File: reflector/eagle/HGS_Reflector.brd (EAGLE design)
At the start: 100 x 100 mm, 42 parts, among them J1 U.FL, J2 USB_MINI-B_SMT, U1 LP2985XX-N, U2 LP2985XX-N

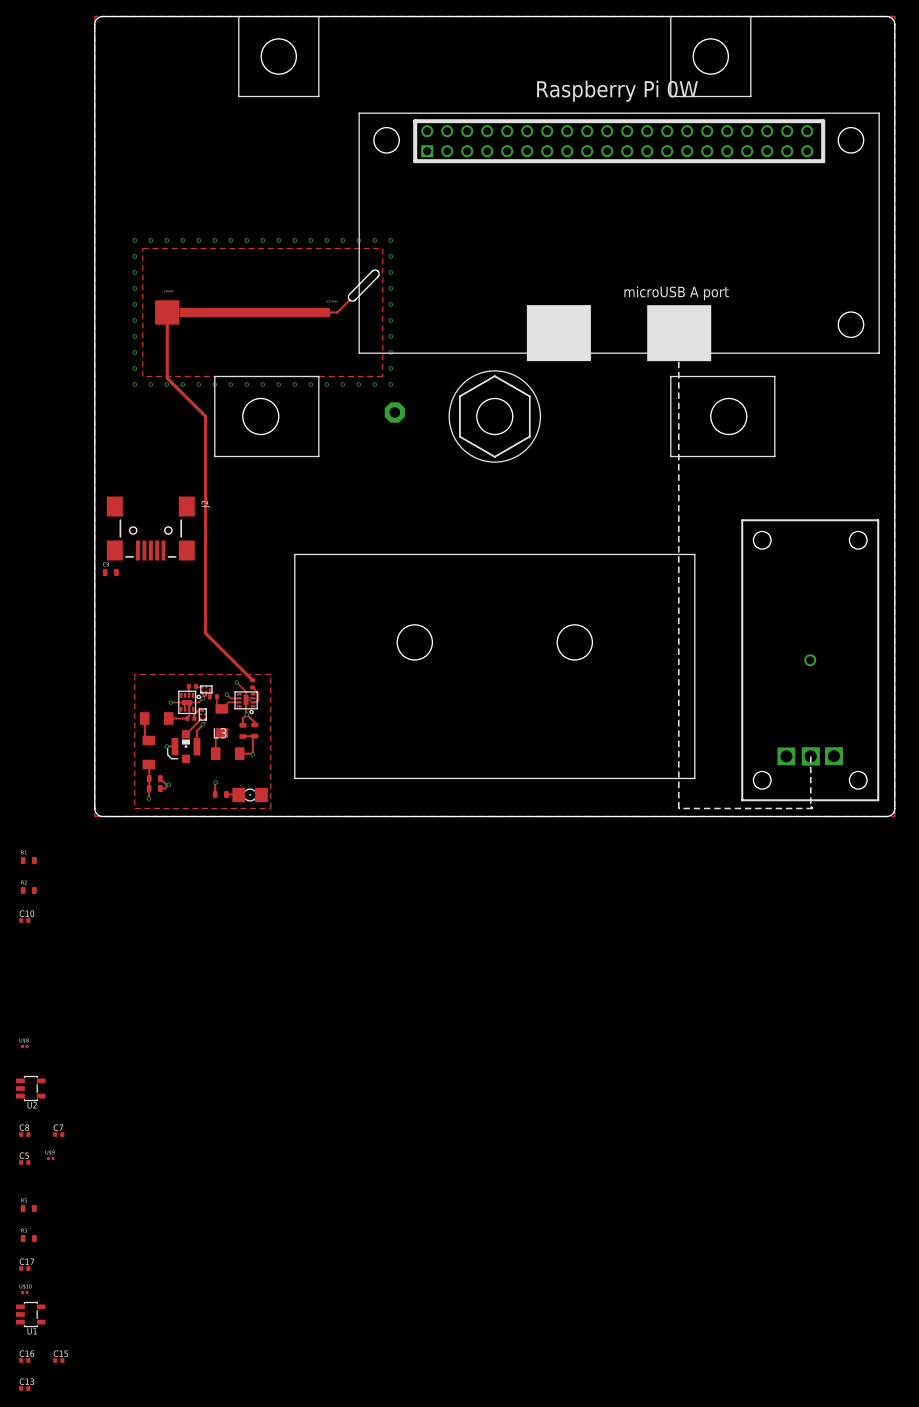
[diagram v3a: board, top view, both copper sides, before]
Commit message: Update for Oliver's series of RF tests to see if we can really do this HGS thing. Took Nohl's board and cleaned it up a bit; the LNA and PS and other things are just for fun; the real purpose of this board is for testing the helical and for testing mechanical fit.
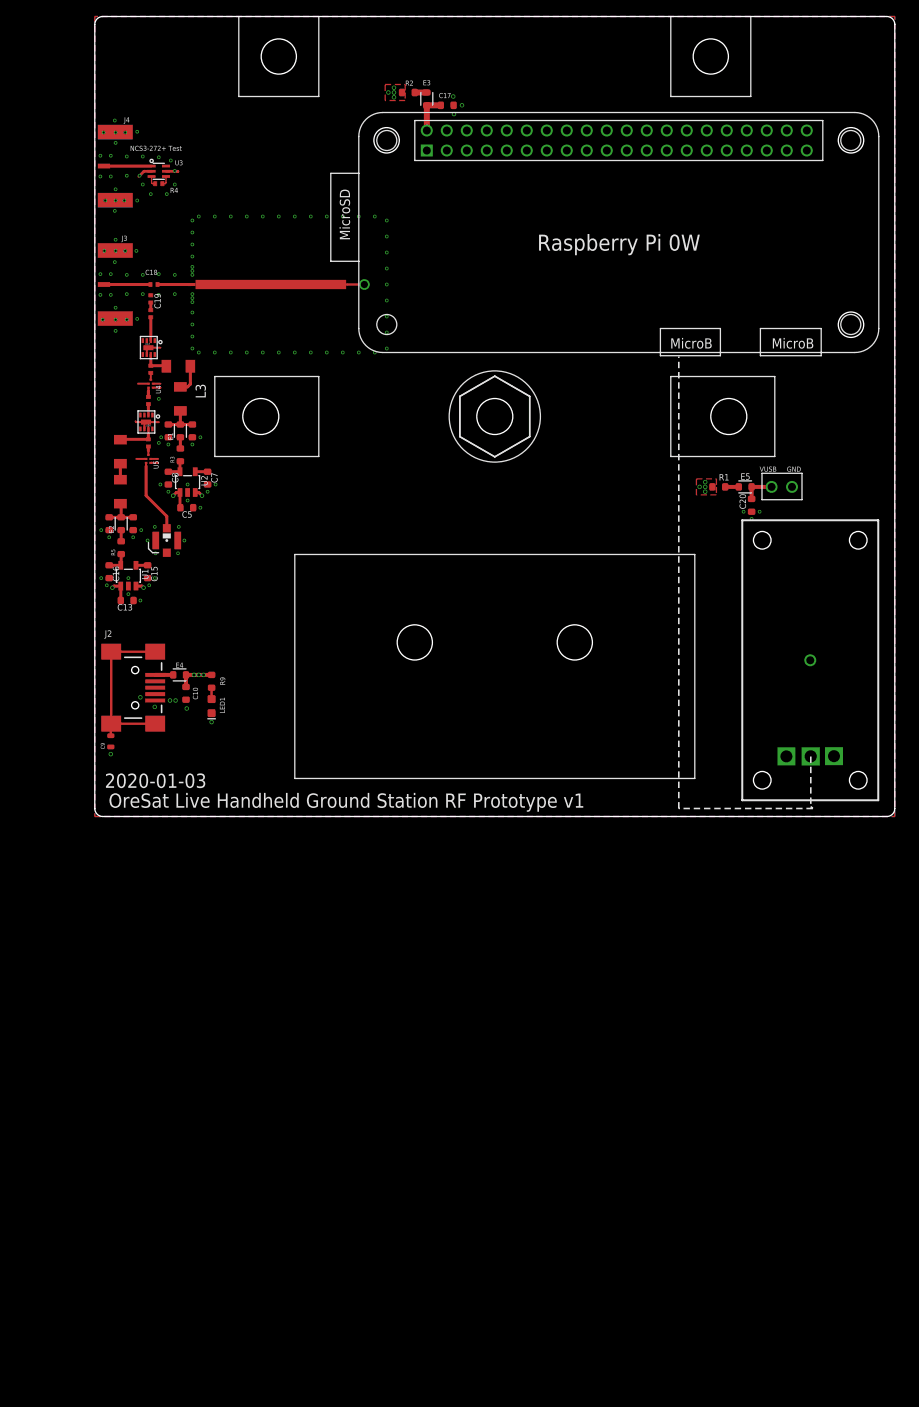
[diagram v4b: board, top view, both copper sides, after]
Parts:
- removed ANT1: (no value), discrete:PAD-01
- removed U$1, U$2: BPF, QPQ1907_BPF:QPQ_1907
- removed U$10, U$8, U$9: FERRITE_BEAD, Ferrite Bead:RESC0603X26N
- removed U$3: QWT2.422, TM-QWT-2.422GHz:QWT_2.422G
- added C18, C19: 100 pF, oresat-rcl:.0402-C-NOSILK
- added C20: 1 uF, oresat-rcl:.0603-B-NOSILK
- added E1, E2, E5: BLM18GG471SZ1D, oresat-rcl:.0603-B
- added E3, E4: BLM18DN381SZ1D, oresat-rcl:.0603-B
- added J3, J4: 142-0701-851, J-Cinch-142-0701-851-SMA-end-launch:142-0701-851
- added R4: 150, oresat-rcl:.0402-C-NOSILK
- added T1: QWT2.4222, TM-QWT-2.422GHz:QWT_2.422G-V2
- added U3: NCS3-272+, U-MiniCirc-NCS3-272+-1-to-3-transformer:GE0805C-1
- added U4, U5: QPQ1907, U-Qorvo-QPQ1907-2.4GHz-BAW-BPF:QPQ1907
- C1, C11, C12, C2: device oresat-rcl:.0603-C-NOSILK -> oresat-rcl:.0603-B-NOSILK
- C10, C13, C15, C16, C17, C5, C7, C8: device oresat-rcl:.0402-C-NOSILK -> oresat-rcl:.0603-B-NOSILK
- L1, L2: value (none) -> 10n
- L3, L4: value (none) -> 8n
- LED1: value (none) -> GREEN; device eagle-ltspice:LED_1206 -> SparkFun-LED:LED-0603
- R1, R2, R3, R5: value FERRITE -> 0; device oresat-rcl:.0603-C-NOSILK -> oresat-rcl:.0603-B-NOSILK
- R9: value 2K -> 1k; device oresat-rcl:.0603-C-NOSILK -> oresat-rcl:.0603-B-NOSILK
- moved C17 154.7 mm to (44.0, 88.9), turned to 180 degrees
- moved R2 110.5 mm to (39.2, 90.5)
- moved R3 99.8 mm to (10.7, 45.2), turned to 90 degrees
- moved C13 99.3 mm to (4.05, 27.0), turned to 180 degrees
- moved C15 99.2 mm to (6.60, 30.6), turned to 270 degrees
- moved C16 99.2 mm to (1.80, 30.6), turned to 270 degrees
- moved R1 98.1 mm to (78.0, 41.2)
- moved U1 93.2 mm to (4.20, 30.1), turned to 90 degrees
- moved C5 84.3 mm to (11.5, 38.6), turned to 180 degrees
- moved C7 84.1 mm to (14.1, 42.3), turned to 270 degrees
- moved C8 84.0 mm to (9.20, 42.3), turned to 270 degrees
- moved R5 83.4 mm to (3.30, 33.6), turned to 90 degrees
- moved U2 78.3 mm to (11.6, 41.8), turned to 90 degrees
- moved C6 48.0 mm to (7.00, 62.9)
- moved U$7 45.7 mm to (6.70, 58.6), turned to 180 degrees
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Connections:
- new net HELICAL: T1.140-IN
- new net N$23: C18.2, J3.RF1
- new net N$24: J4.RF1, U3.1
- new net N$26: R4.2, U3.3
- new net N$27: R4.1, U3.4
- new net N$28: C19.2, C6.1
- new net N$29: C20.2, E5.2
- new net N$30: E5.1, R1.2
- new net T1-50: C18.1, T1.50-OUT
- net GND: now also C19.1, C20.1, J3.GND1, J3.GND2, J3.GND3, J3.GND4, J4.GND1, J4.GND2, J4.GND3, J4.GND4, U3.2, U3.5, U4.GND, U4.GND2, U4.GND3, U5.GND, U5.GND2, U5.GND3; no longer U$1.GND, U$1.GND2, U$1.GND3, U$2.GND, U$2.GND2, U$2.GND3
- net N$15: now also E3.2; no longer U$10.2
- net N$17: now also E4.1; no longer R1.2
- net N$18: now also E3.1; no longer U$10.1
- net N$2: now also E1.1, R3.2; no longer U$3.P$2
- net N$20: now also E1.2; no longer U$9.2
- net N$21: now also E2.2; no longer U$8.2
- net N$3: now also U5.INPUT; no longer U$2.INPUT
- net N$4: now also U4.OUTPUT; no longer U$1.OUTPUT
- net N$5: now also U5.OUTPUT; no longer U$2.OUTPUT
- net N$6: now also U4.INPUT; no longer U$1.INPUT
- net N$9: now also E2.1, R5.2; no longer C6.1, U$3.P$1
- net VUSB: now also E4.2
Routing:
- net N$9: track 50.4 -> 1.40 mm
- net N$12: track 0.00 -> 23.9 mm
- net VUSB: track 1.52 -> 12.6 mm, vias 1 -> 15
- net GND: track 23.4 -> 15.8 mm, vias 58 -> 142
- net N$5: track 2.74 -> 9.27 mm
- net N$24: track 0.00 -> 5.95 mm
- net N$23: track 0.00 -> 5.80 mm
- net N$15: track 0.00 -> 4.90 mm
- net T1-50: track 0.00 -> 4.23 mm
- net N$29: track 0.00 -> 4.00 mm, vias 0 -> 1
- net N$22: track 0.00 -> 2.87 mm
- net N$25: track 0.00 -> 2.77 mm
- net N$17: track 0.00 -> 2.25 mm
- net HELICAL: track 0.00 -> 2.15 mm, vias 0 -> 1
- net N$30: track 0.00 -> 1.70 mm
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- added copper zone on layer 15, net ALKSJDLAKS
- added copper zone on layer 1, net VUSB
- added copper zone on layer 15, net VUSB
- removed copper zone on layer 15, net 3.3V
- removed copper zone on layer 1, net KEEPOUT
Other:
- outline, holes or cut-outs redrawn
- board text added: "2020-01-03"
- board text added: "GND"
- board text added: "NCS3-272+ Test"
- board text added: "OreSat Live Handheld Ground Station RF Prototype v1"
- board text added: "VUSB"

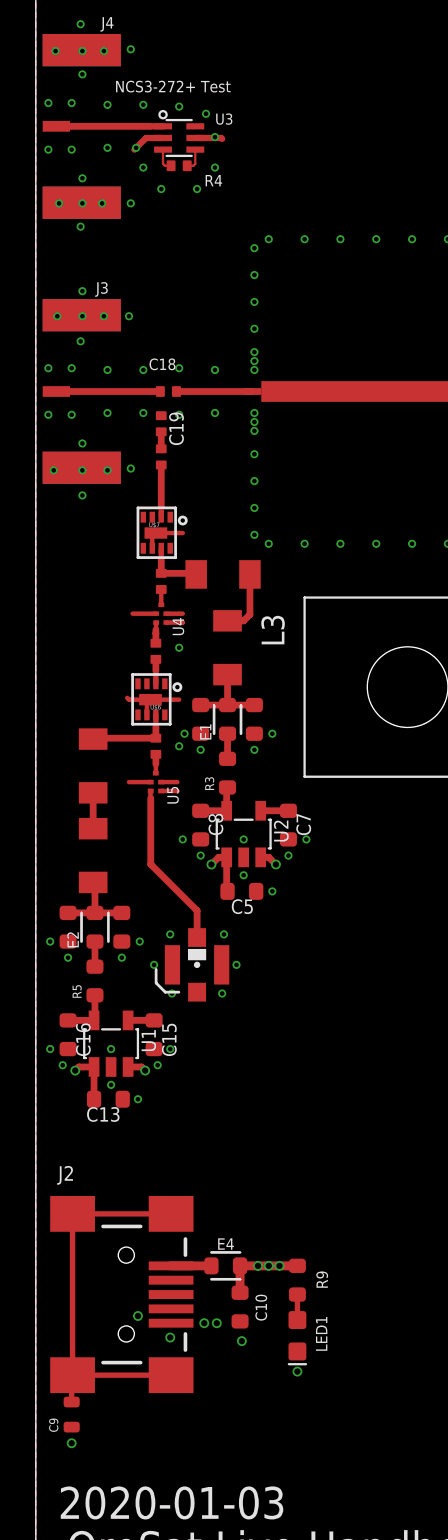
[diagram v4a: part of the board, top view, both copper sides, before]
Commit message: TNAMES polish, ran DRC and ERCs. Not ready for prime time, but OK for v1.
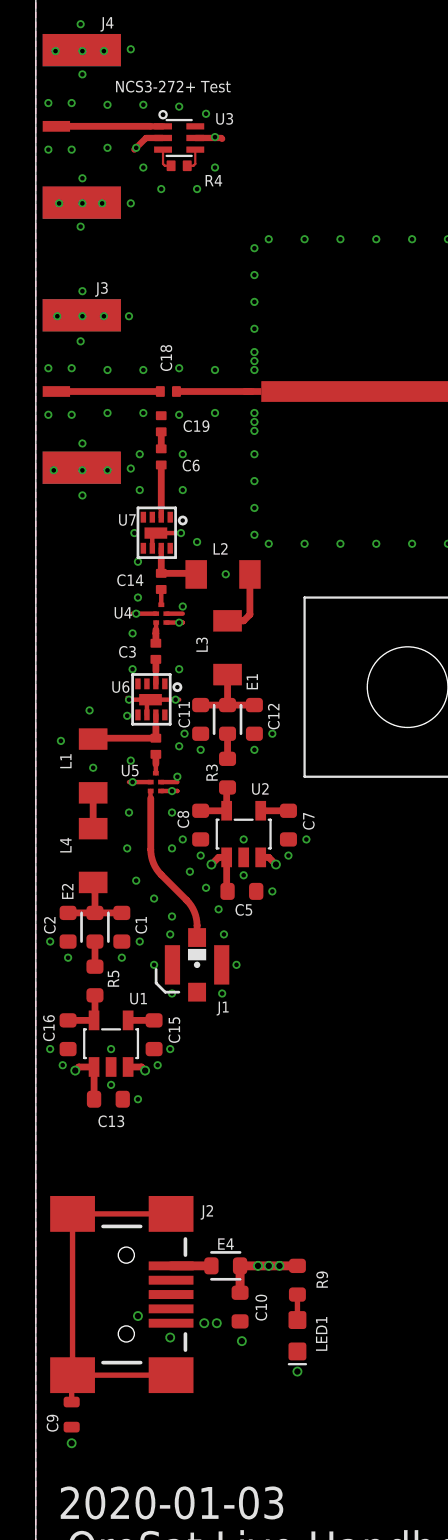
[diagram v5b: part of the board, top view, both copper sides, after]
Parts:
- renumbered U$6 to U6, U$7 to U7
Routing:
- net GND: vias 142 -> 177

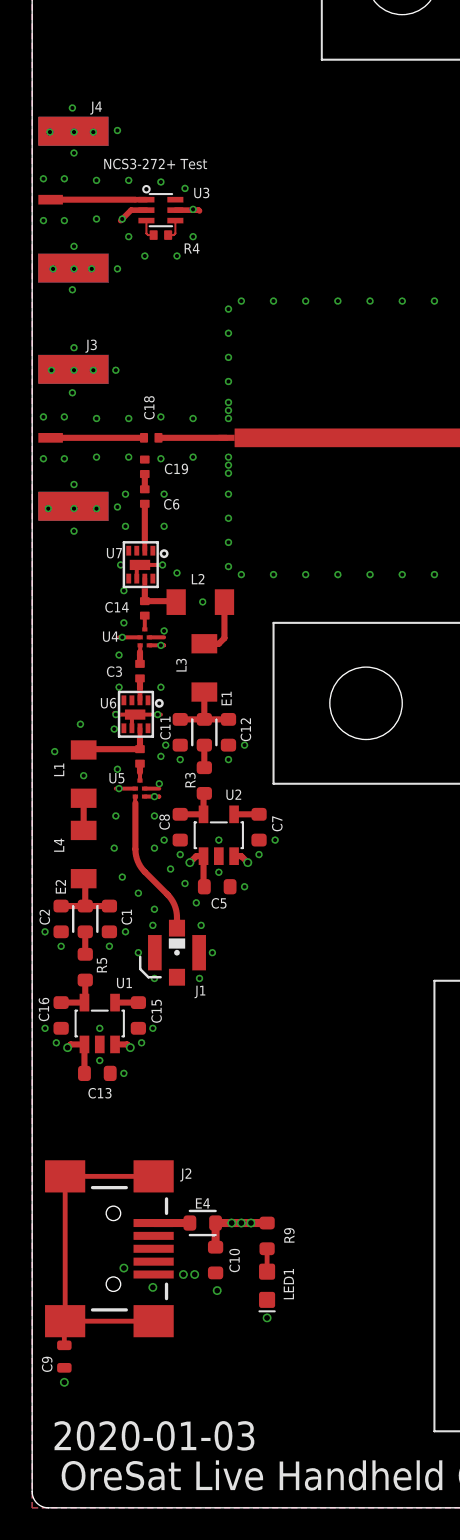
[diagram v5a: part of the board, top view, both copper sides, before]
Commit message: Switched edge fired SMA connectors to Oliver's fancy SMT vertical connectors.
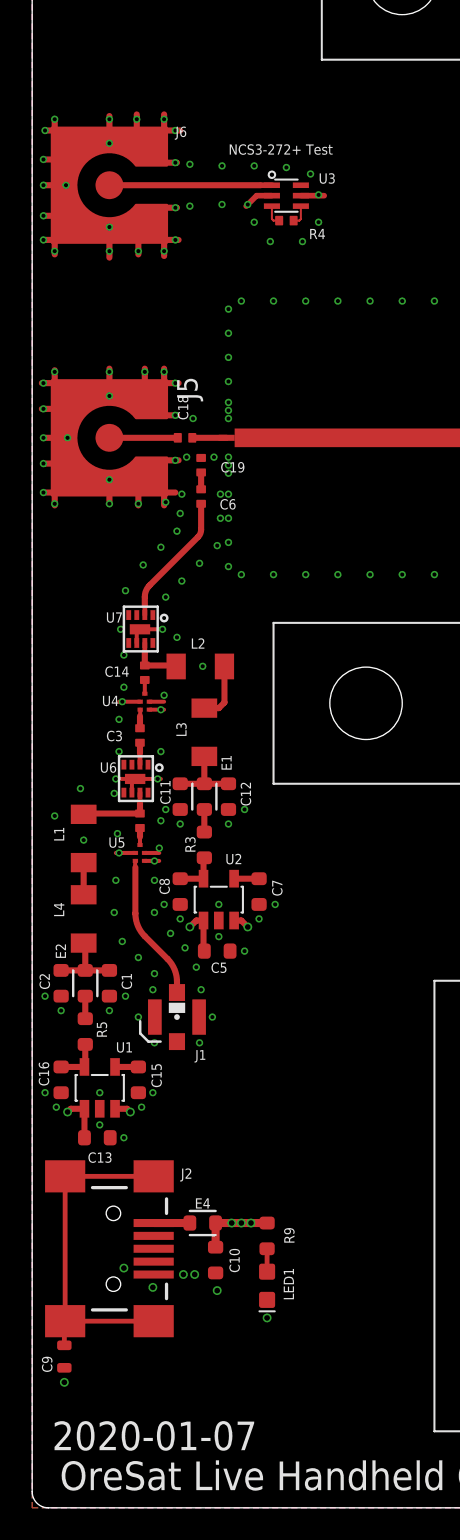
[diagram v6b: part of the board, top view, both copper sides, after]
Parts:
- removed J3, J4: 142-0701-851, J-Cinch-142-0701-851-SMA-end-launch:142-0701-851
- added J5, J6: 132134-10, J-Amphenol-132134-10-SMA-F-SMT-vertical:132134-10
- moved R4 7.85 mm to (15.8, 80.0)
- moved U3 7.85 mm to (15.8, 81.5)
- moved C1 4.00 mm to (4.80, 32.6)
- moved C11 4.00 mm to (9.20, 44.2)
- moved C12 4.00 mm to (12.2, 44.2)
- moved C13 4.00 mm to (4.05, 23.0)
- moved C14 4.00 mm to (7.00, 51.9)
- moved C15 4.00 mm to (6.60, 26.6)
- moved C16 4.00 mm to (1.80, 26.6)
- moved C2 4.00 mm to (1.80, 32.6)
- moved C3 4.00 mm to (6.70, 48.0)
- moved C4 4.00 mm to (6.70, 42.7)
- moved C5 4.00 mm to (11.5, 34.6)
- moved C7 4.00 mm to (14.1, 38.3)
- moved C8 4.00 mm to (9.20, 38.3)
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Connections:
- net GND: now also J5.SHIELD, J6.SHIELD; no longer J3.GND1, J3.GND2, J3.GND3, J3.GND4, J4.GND1, J4.GND2, J4.GND3, J4.GND4
- net N$23: now also J5.CENTER; no longer J3.RF1
- net N$24: now also J6.CENTER; no longer J4.RF1
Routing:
- net GND: track 15.8 -> 49.6 mm, vias 177 -> 189
- net N$11: track 2.92 -> 8.26 mm
- net N$24: track 5.95 -> 10.1 mm
- net T1-50: track 4.23 -> 2.13 mm
- net N$23: track 5.80 -> 4.25 mm
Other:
- board text added: "2020-01-07"
- board text removed: "2020-01-03"

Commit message: Added more stitching to RF connectors, and added possible connection to the WF Atheros card... might work? Might not? First round try!
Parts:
- removed U$4: AR9721WF, AR9721:WF-NP9202
- added C21: 100 pF, oresat-rcl:.0603-C-NOSILK
- added J3: SM06B-SRSS-TB(LF)(SN), J-JST-SM06B-SRSS-TB(LF)(SN)-1mm-smt-6pin:CONN_SM06B-SRSS-TB_JST
- added LED2: GREEN, SparkFun-LED:LED-0603
- added PCBA1: WF-NP9202WF, PCBA-WF-NP9202-wifi-adapter:WF-NP9202
- added R6: 0, oresat-rcl:.0603-B-NOSILK
- added R7: 1k, oresat-rcl:.0603-B-NOSILK
- added TP2: TEST-POINT-LARGE-SQUARE, oresat-misc:1X01
- added X1: (no value), BeagleBone_Blue_R3:GHI2_USB_HOST_HORIZONTAL_W/CHASSIS_GND
- moved C20 25.4 mm to (56.9, 41.8), turned to 0 degrees
- moved E5 22.1 mm to (59.2, 42.6), turned to 270 degrees
- moved R1 19.4 mm to (59.2, 45.9), turned to 270 degrees
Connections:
- new net N$31: J3.6, R6.2
- new net N$32: LED2.A, R7.1
- new net N$33: J3.2, X1.3
- new net N$34: J3.5, LED2.C
- new net N$36: J3.3, X1.2
- new net N$37: TP2.1, X1.1
- new net N$38: C21.2, X1.5, X1.6
- net GND: now also C21.1, J3.4, J3.7, J3.8, X1.4
- net N$29: now also J3.1, R6.1, R7.2
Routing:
- net N$33: track 0.00 -> 25.6 mm
- net N$36: track 0.00 -> 24.4 mm, vias 0 -> 1
- net N$29: track 4.00 -> 20.0 mm
- net N$38: track 0.00 -> 16.0 mm
- net N$34: track 0.00 -> 4.86 mm
- net N$37: track 0.00 -> 2.91 mm
- net N$32: track 0.00 -> 2.43 mm
- net N$31: track 0.00 -> 2.09 mm
- net GND: vias 189 -> 201

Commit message: Part and BOM cleanup
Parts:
- C1, C11, C12, C2: device oresat-rcl:.0603-B-NOSILK -> oresat-rcl:.0603-C-NOSILK
- renumbered U$5 to PCBA2, X1 to J7
